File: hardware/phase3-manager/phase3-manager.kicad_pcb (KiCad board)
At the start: 2 copper layers, 100 x 80 mm, 86 parts, among them J1 BACKPLANE, J3 USB-C, J4 UART, J5 PANEL KEYS, J6 ILI9341 LCD MODULE, Q10 2N7002, Q11 AO3401A-class PMOS, Q8 2N7002, Q9 2N7002, SW1 RESET, SW2 BOOT, U10 ESP32-S3-WROOM-1-N8R2, U11 TCAN1042HGV, U12 TPD2E001, U13 TCA9535PWR, U8 LMR36015AQRNXRQ1, U9 NCP1117-3.3

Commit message: Manager board: fix two real defects found by kicad-happy audit
Ran the audit stack (schematic, PCB --full, cross-domain, EMC, thermal,
SPICE) that this project uses at milestones but that the new board had
never seen. It found two genuine layout defects, both introduced while
iterating placement against courtyard collisions:

 * EMC DC-002 (error): U10 sat 19.3 mm from its own decoupling. Its 3V3
   pin is pad 2 at the module's TOP-left (61.2, 17.0), not the bottom
   where I had assumed; an earlier pass parked C64/C65 at y=36 to clear
   the courtyard. Moved beside the pin — 3.0 mm and 5.5 mm, both still
   clear of the antenna keep-out. Error cleared.
 * EMC SW-003: the buck's input caps were 23 mm from U8, the classic
   large-hot-loop error — SW-003 scores the cap/IC/inductor triangle and
   wants <25 mm2. C50/C51 now hug U8's VIN pads at 2.6 / 4.8 mm. Cleared.

Also added: a board-level rule area over the antenna (the footprint's own
keep-out already works — verified by flooding the planes and sampling 611
interior points, 0 with copper — but a board-level area makes the
constraint visible to the analyzers and survives a footprint swap), and a
third fiducial for FD-001 (SMD assembly wants >=3 per side).

Board still 0 DRC. EMC risk 97/100, 0 errors. Thermal: U9 Tj 58 C with
67 C margin. Cross-domain: 0 findings.

Backplane audited too — every warning triaged to a false positive against
the actual fabrication output: VP-001 "untented via-in-pad" (F_Mask has
no opening at any of the three sites — they ARE tented), GR-002 layer
alignment (copper legitimately inset from the edge), GR-004 paste count
(28 flashes matches the SMD count exactly; the rest is THT). No blockers.

Co-Authored-By: Claude Fable 5 <noreply@anthropic.com>
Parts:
- added FID3: Fiducial, Fiducial:Fiducial_1mm_Mask2mm, F.Cu at (110.0, 96.0)
- moved C51 22.8 mm to (43.0, 70.5)
- moved C65 20.4 mm to (78.3, 37.0)
- moved C50 19.7 mm to (43.0, 74.5)
- moved C64 16.1 mm to (77.0, 40.5)

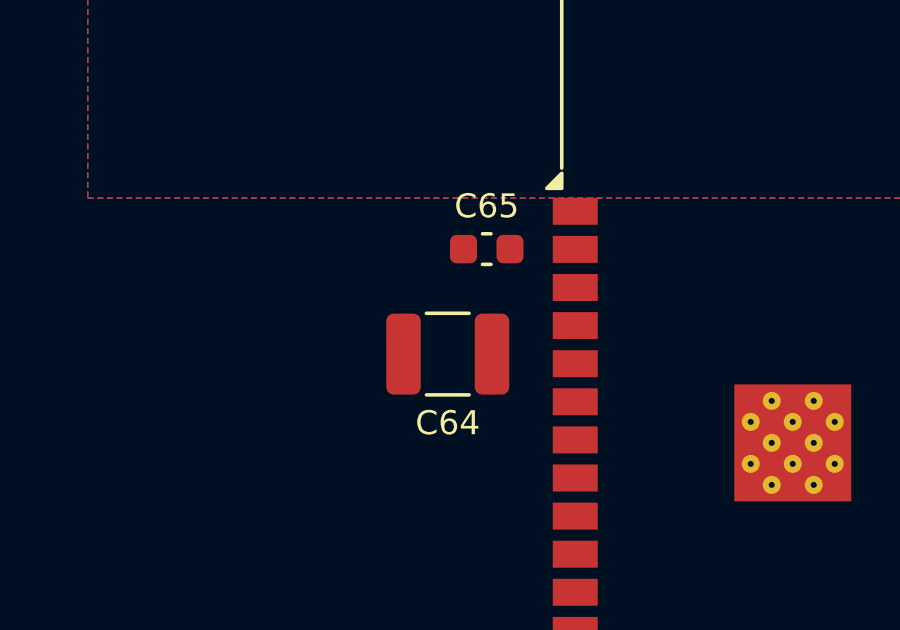
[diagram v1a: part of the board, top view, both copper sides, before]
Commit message: Manager 3V3 plane break + five tooling defects, from a 9-commit review
Reviewed 8010576..9a8feb8 and re-measured every headline number
independently. The claims hold: phase-1 75 silk/187 unconnected, phase-2 11
silk/83 unconnected, backplane 0/0, manager 0 DRC; the lib_footprint_issues
fix is real (0 Footprint errors on every board now) and the phase-1 board
diff in d9e1a7b was FPID-only, nothing else disturbed. fix_fpids' guessing
risk is a non-issue here: 13,494 footprint names indexed, 0 in >1 library.

One real regression, though, and it was in the newest commit.

MANAGER 3V3 PLANE WAS SEVERED (regression in 9a8feb8)

Moving C64/C65 beside U10 to clear EMC DC-002 pinched the F.Cu 3V3 pour in
two: 1 contiguous outline of 5831.68 mm2 became 5588.13 + a 244.64 mm2
ISLAND carrying U10's own 3V3 pad with no via/PTH tie. At rot 0 those caps
face U10 with their PGND pad, 0.97 mm from U10's pad column, and at 0.3 mm
zone clearance per side that channel cannot fill.

What makes it worth a commit message this long is how it hid: the board
still passed DRC at 0 violations, and the break surfaced only as ONE extra
unconnected item (173 -> 174) buried in an unrouted signal-net list.

Fixed by turning both caps round — 3V3 pad faces U10, so the gap is same-net
and the pour flows through it. Strictly better than what it replaces on both
EMC distances: C65 3.73 -> 2.68 mm, C64 6.70 -> 4.79 mm from pad 2. Measured
alternatives are recorded in place (rot 0 + 1.0 mm left also heals the plane
but costs distance; rot 180 alone does not heal it — it needs the x too).

  3V3 F.Cu    2 outlines -> 1 contiguous, 5833.41 mm2
  unconnected 174 -> 173
  DRC         0 violations, 0 footprint errors (unchanged)
  keep-out    0 filled-copper vertices inside the antenna zone (unchanged)

check_plane_continuity() now fails the build on any pour fragment that holds
pads without a tie. It runs AFTER the final fill, because island geometry is
a property of the finished copper, not of the zone outl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
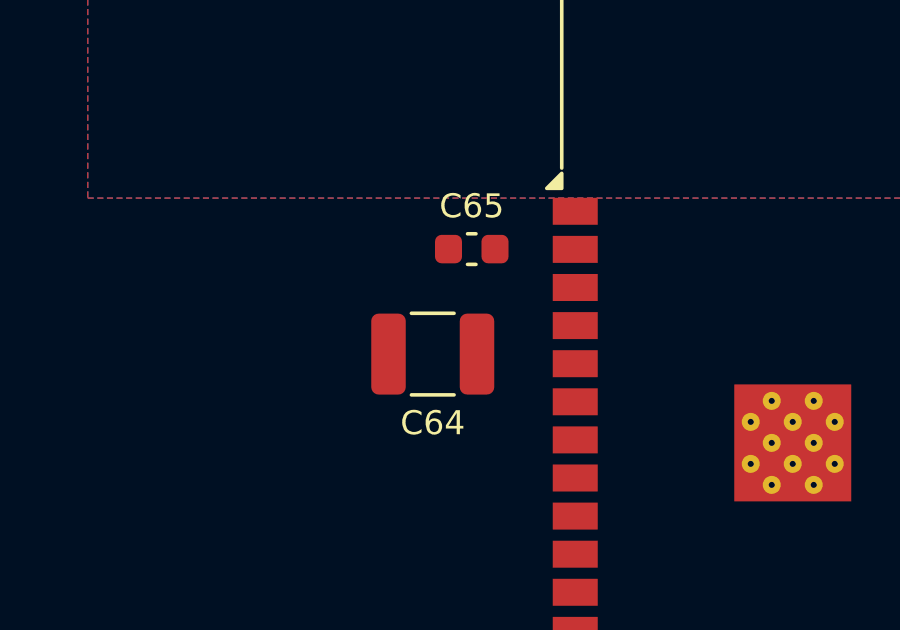
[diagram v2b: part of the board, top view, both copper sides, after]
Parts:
- moved C64 0.50 mm to (76.5, 40.5), turned to 180 degrees
- moved C65 0.50 mm to (77.8, 37.0), turned to 180 degrees
